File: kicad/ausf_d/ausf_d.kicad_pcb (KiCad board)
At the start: 2 copper layers, 100 x 48 mm, 44 parts, among them J1 Jack-DC, J2 Conn_01x02_Male, J3 Conn_02x10_Odd_Even, J4 Conn_01x02, Q1 IRF640, Q2 2SD669AD-C, Q3 BC847, Q4 BC847, T1 TRIM_EU-S64W, U1 max1771, U2 MC34063AP, U3 ESP-12F, U4 AMS1117CD-3.3

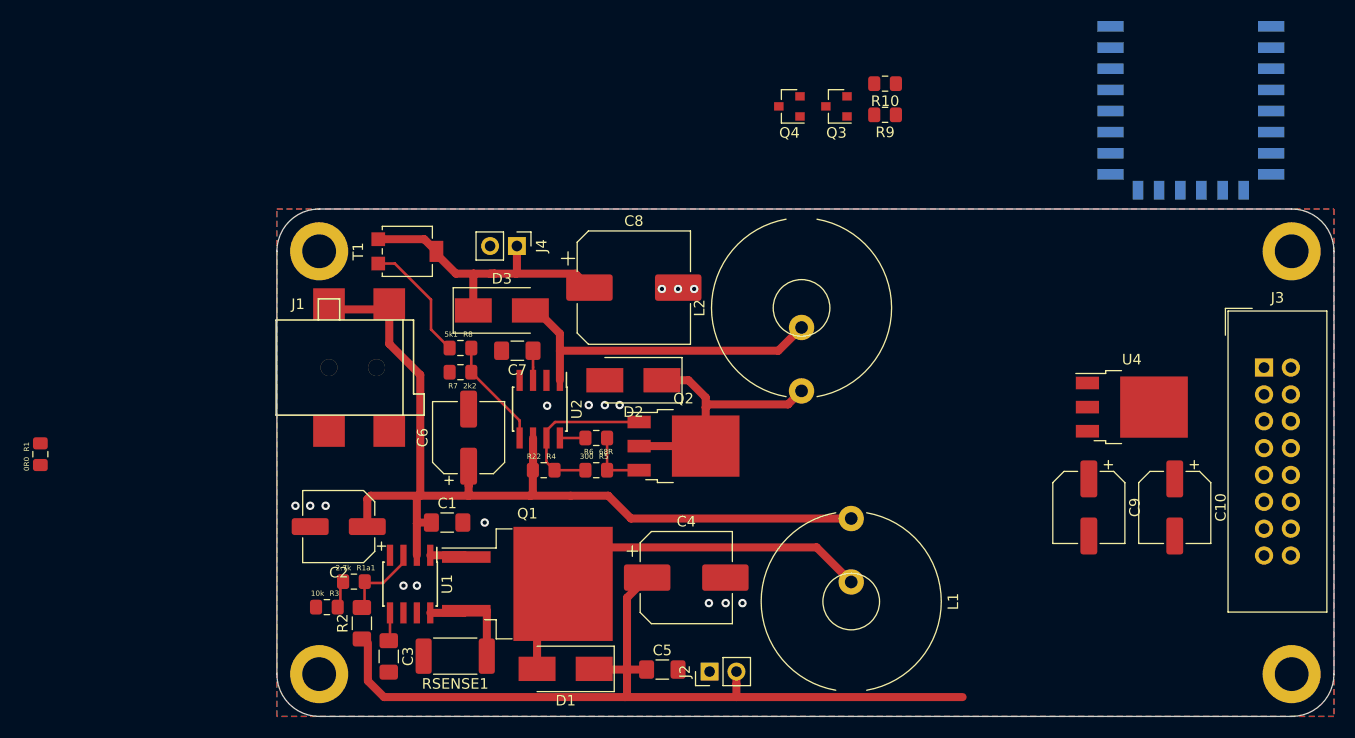
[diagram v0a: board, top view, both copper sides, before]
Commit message: Made version work with Ausf. A and Ausf. C
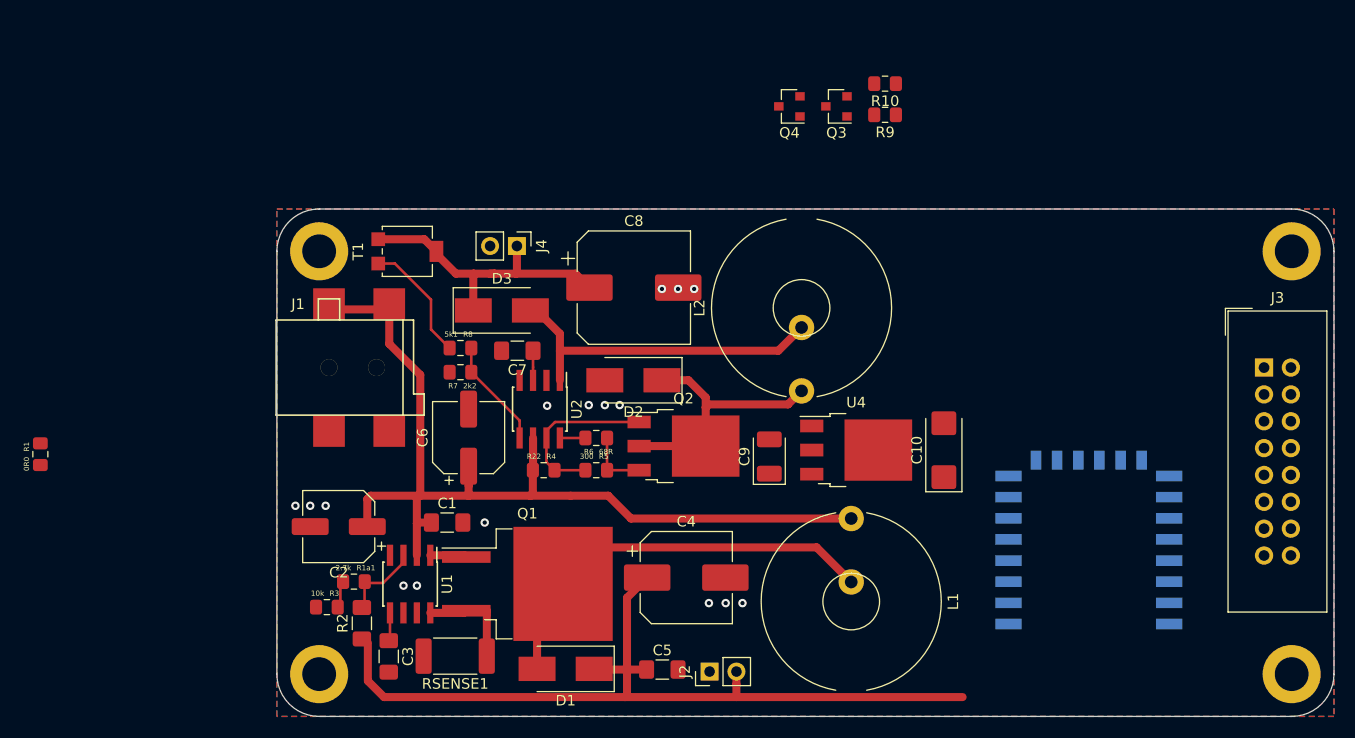
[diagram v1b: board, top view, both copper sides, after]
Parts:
- C10: footprint Capacitor_SMD:CP_Elec_6.3x5.8 -> Capacitor_Tantalum_SMD:CP_EIA-6032-28_Kemet-C_Pad2.25x2.35mm_HandSolder
- C9: footprint Capacitor_SMD:CP_Elec_6.3x5.8 -> Capacitor_Tantalum_SMD:CP_EIA-3528-12_Kemet-T_Pad1.50x2.35mm_HandSolder
- moved U3 50.5 mm to (146.8, 95.8), turned to 0 degrees
- moved C9 30.6 mm to (116.6, 83.4), turned to 90 degrees
- moved U4 26.4 mm to (124.8, 82.8)
- moved C10 22.5 mm to (133.1, 82.8), turned to 90 degrees
